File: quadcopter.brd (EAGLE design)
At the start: 137.3 x 137.3 mm, 72 parts, among them J1 AVR_SPI_PRG_6NS, U1 ATMEGA128RFA1, Y2 16MHz

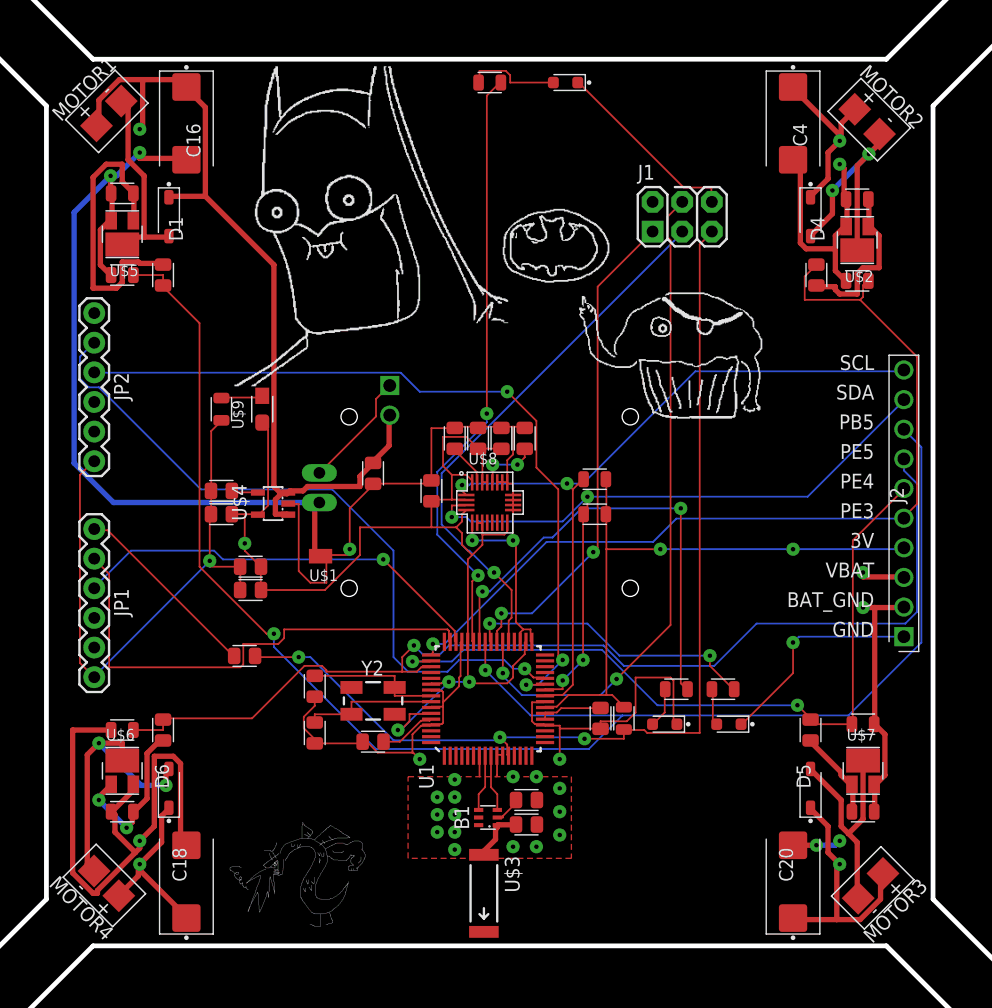
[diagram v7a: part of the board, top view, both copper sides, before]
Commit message: Fixed issues found by Swanson's review, board ready to be auto-routed
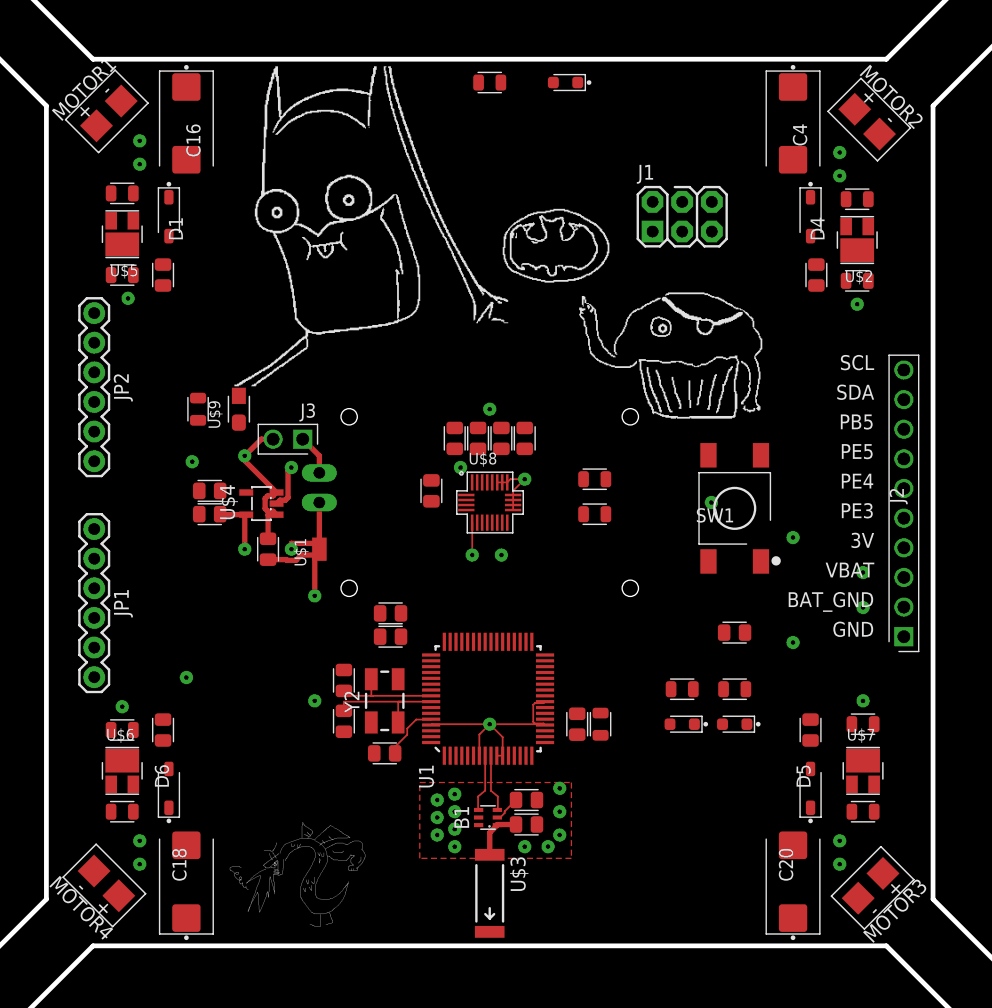
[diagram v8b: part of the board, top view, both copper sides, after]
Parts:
- added SW1: PUSHBUTTON_SMD-VERTICAL-1, quadparts_prebuilt:TE_FSM8JSMA_HS
- moved C13 42.0 mm to (59.0, 26.9)
- moved C11 12.6 mm to (29.5, 26.5)
- moved C12 12.6 mm to (29.5, 28.5)
- moved C2 11.1 mm to (19.0, 34.0)
- moved J3 8.76 mm to (22.0, 43.4), flipped to the top, turned to 180 degrees
- moved C6 2.69 mm to (25.5, 19.2)
- moved C5 2.55 mm to (25.5, 22.8), turned to 90 degrees
- moved C7 2.06 mm to (45.5, 19.0)
- moved R5 2.06 mm to (47.5, 19.0)
- moved R15 2.00 mm to (13.0, 46.0)
- moved U$9 2.00 mm to (16.5, 46.0)
- moved D3 1.50 mm to (54.5, 19.0)
- moved C8 1.41 mm to (29.0, 16.5)
- moved C14 1.00 mm to (14.0, 39.0)
- moved C3 1.00 mm to (14.0, 37.0)
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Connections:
- net GND: now also SW1.3, SW1.4
- net RESET: now also SW1.1, SW1.2
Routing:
- net GND: track 212.5 -> 41.0 mm, vias 22 -> 23
- net BAT_GND: track 168.1 -> 6.40 mm, vias 7 -> 10
- net 3V: track 156.0 -> 5.36 mm, vias 6 -> 4
- net PB5: track 136.3 -> 0.00 mm, vias 2 -> 0
- net VBAT: track 130.5 -> 13.3 mm, vias 5 -> 6
- net PE5: track 91.5 -> 0.00 mm, vias 1 -> 0
- net RESET: track 87.5 -> 0.00 mm, vias 3 -> 0
- net PE3: track 77.2 -> 0.00 mm, vias 1 -> 0
- net RX1: track 66.7 -> 0.00 mm, vias 3 -> 0
- net PE4: track 64.7 -> 0.00 mm, vias 2 -> 0
- net SCL: track 64.6 -> 0.00 mm, vias 2 -> 0
- net SDA: track 64.5 -> 0.00 mm, vias 4 -> 0
- net TX1: track 60.3 -> 0.00 mm, vias 1 -> 0
- net MOSI: track 57.4 -> 0.00 mm, vias 2 -> 0
- net PB7: track 52.0 -> 0.00 mm, vias 2 -> 0
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- removed copper zone on layer 15, net N$15
